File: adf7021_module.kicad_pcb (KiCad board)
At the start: 4 copper layers, 52 x 26 mm, 70 parts, among them J1 Conn_02x10_Counter_Clockwise, J2 Conn_Coaxial, J3 Conn_Coaxial, J4 Conn_02x10_Counter_Clockwise, J5 Conn_Coaxial, J6 Conn_Coaxial, U1 ADF7021, X1 19.68MHz

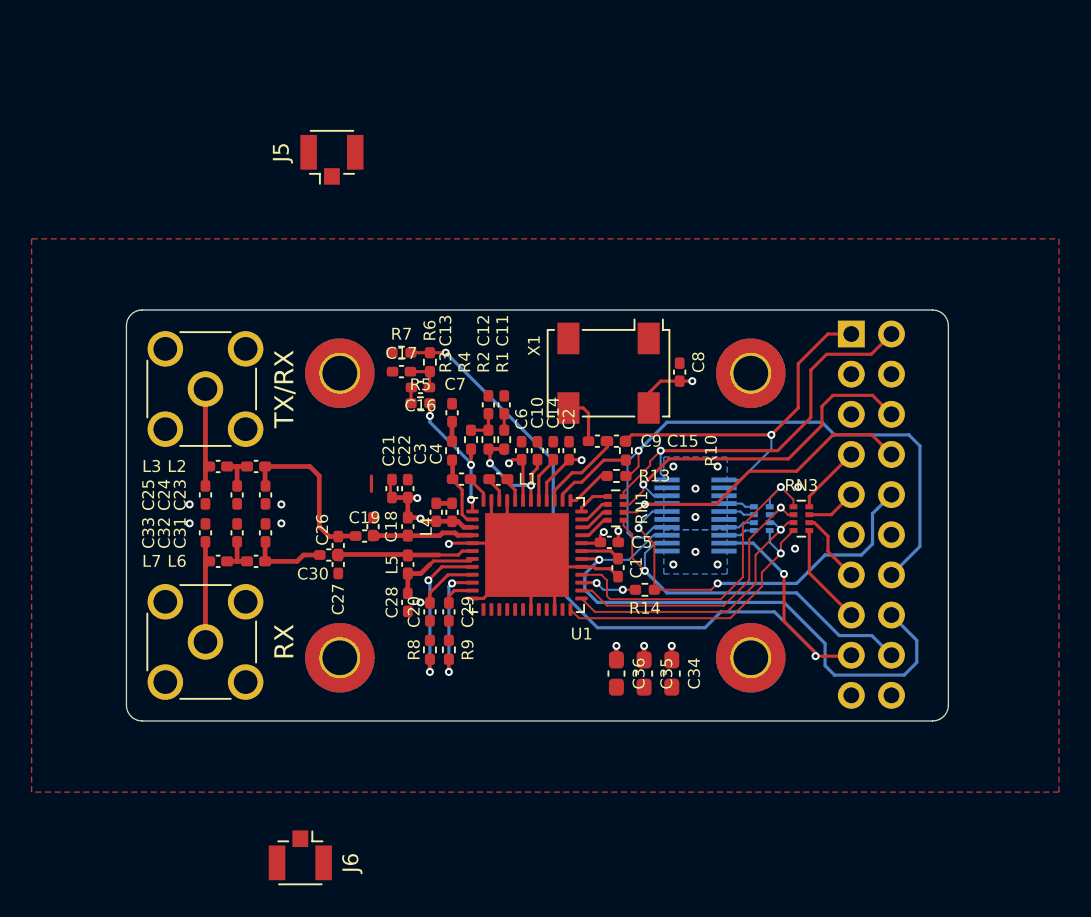
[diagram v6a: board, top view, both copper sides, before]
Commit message: Adding pinout silkscreen
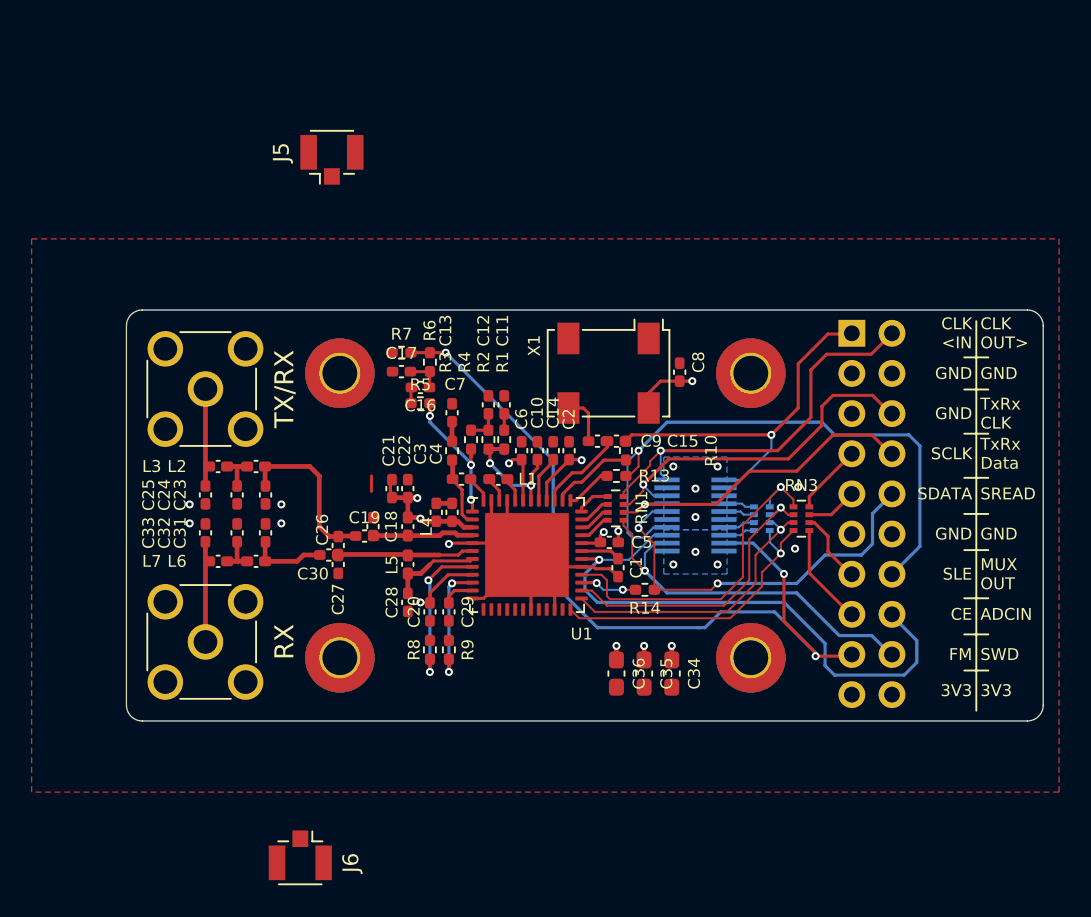
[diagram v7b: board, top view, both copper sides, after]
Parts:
- moved J4 0.06 mm to (151.9, 46.0)
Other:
- board size 52 x 26 mm -> 58 x 26 mm
- board text added: "3V3"
- board text added: "ADCIN"
- board text added: "CE"
- board text added: "CLK <IN"
- board text added: "CLK OUT>"
- board text added: "FM"
- board text added: "GND"
- board text added: "MUX OUT"
- board text added: "SCLK"
- board text added: "SDATA"
- board text added: "SLE"
- board text added: "SREAD"
- board text added: "SWD"
- board text added: "TxRx CLK"
- board text added: "TxRx Data"
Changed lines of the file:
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@@
   (general
     (thickness 1.6)
-    (drawings 20)
+    (drawings 50)
     (tracks 452)
     (zones 0)
@@
   )
   (module Connector_PinSocket_2.54mm:PinSocket_2x10_P2.54mm_Vertical (layer B.Cu)
-    (at 151.86 46.02 180)
+    (at 151.892 45.974 180)
     (descr "Through hole straight socket strip, 2x10, 2.54mm pitch, double cols (from Kicad 4.0.7), script generated")
     (tags "Through hole socket strip THT 2x10 2.54mm double row")
@@
     )
   )
+  (gr_line (start 159.004 47.498) (end 160.528 47.498) (layer F.SilkS) (width 0.12))
+  (gr_line (start 159.004 49.53) (end 160.528 49.53) (layer F.SilkS) (width 0.12))
+  (gr_line (start 159.004 52.324) (end 160.528 52.324) (layer F.SilkS) (width 0.12))
+  (gr_line (start 159.004 55.118) (end 160.528 55.118) (layer F.SilkS) (width 0.12))
+  (gr_line (start 159.004 57.404) (end 160.528 57.404) (layer F.SilkS) (width 0.12))
+  (gr_line (start 159.004 59.69) (end 160.528 59.69) (layer F.SilkS) (width 0.12))
+  (gr_line (start 159.004 62.738) (end 160.528 62.738) (layer F.SilkS) (width 0.12))
+  (gr_line (start 159.004 65.024) (end 160.528 65.024) (layer F.SilkS) (width 0.12))
+  (gr_line (start 159.004 67.31) (end 160.528 67.31) (layer F.SilkS) (width 0.12))
+  (gr_line (start 159.766 45.212) (end 159.766 69.85) (layer F.SilkS) (width 0.12))
+  (gr_text 3V3 (at 160.02 68.58) (layer F.SilkS)
+    (effects (font (size 0.75 0.75) (thickness 0.15)) (justify left))
+  )
+  (gr_text SWD (at 160.02 66.294) (layer F.SilkS)
+    (effects (font (size 0.75 0.75) (thickness 0.15)) (justify left))
+  )
+  (gr_text ADCIN (at 160.02 63.754) (layer F.SilkS)
+    (effects (font (size 0.75 0.75) (thickness 0.15)) (justify left))
+  )
+  (gr_text "MUX\nOUT" (at 160.02 61.214) (layer F.SilkS)
+    (effects (font (size 0.75 0.75) (thickness 0.15)) (justify left))
+  )
+  (gr_text GND (at 160.02 58.674) (layer F.SilkS)
+    (effects (font (size 0.75 0.75) (thickness 0.15)) (justify left))
+  )
+  (gr_text SREAD (at 160.02 56.134) (layer F.SilkS)
+    (effects (font (size 0.75 0.75) (thickness 0.15)) (justify left))
+  )
+  (gr_text "TxRx\nData" (at 160.02 53.594) (layer F.SilkS)
+    (effects (font (size 0.75 0.75) (thickness 0.15)) (justify left))
+  )
+  (gr_text "TxRx\nCLK" (at 160.02 51.054) (layer F.SilkS)
+    (effects (font (size 0.75 0.75) (thickness 0.15)) (justify left))
+  )
+  (gr_text GND (at 160.02 48.514) (layer F.SilkS)
+    (effects (font (size 0.75 0.75) (thickness 0.15)) (justify left))
+  )
+  (gr_text "CLK\nOUT>" (at 160.02 45.974) (layer F.SilkS)
+    (effects (font (size 0.75 0.75) (thickness 0.15)) (justify left))
+  )
+  (gr_text 3V3 (at 159.512 68.58) (layer F.SilkS)
+    (effects (font (size 0.75 0.75) (thickness 0.15)) (justify right))
+  )
+  (gr_text FM (at 159.512 66.294) (layer F.SilkS)
+    (effects (font (size 0.75 0.75) (thickness 0.15)) (justify right))
+  )
+  (gr_text CE (at 159.512 63.754) (layer F.SilkS)
+    (effects (font (size 0.75 0.75) (thickness 0.15)) (justify right))
+  )
+  (gr_text SLE (at 159.512 61.214) (layer F.SilkS)
+    (effects (font (size 0.75 0.75) (thickness 0.15)) (justify right))
+  )
+  (gr_text GND (at 159.512 58.674) (layer F.SilkS)
+    (effects (font (size 0.75 0.75) (thickness 0.15)) (justify right))
+  )
+  (gr_text SDATA (at 159.512 56.134) (layer F.SilkS)
+    (effects (font (size 0.75 0.75) (thickness 0.15)) (justify right))
+  )
+  (gr_text SCLK (at 159.512 53.594) (layer F.SilkS)
+    (effects (font (size 0.75 0.75) (thickness 0.15)) (justify right))
+  )
+  (gr_text GND (at 159.512 51.054) (layer F.SilkS)
+    (effects (font (size 0.75 0.75) (thickness 0.15)) (justify right))
+  )
+  (gr_text GND (at 159.512 48.514) (layer F.SilkS)
+    (effects (font (size 0.75 0.75) (thickness 0.15)) (justify right))
+  )
+  (gr_text "CLK\n<IN" (at 159.512 45.974) (layer F.SilkS)
+    (effects (font (size 0.75 0.75) (thickness 0.15)) (justify right))
+  )
   (gr_text RX (at 116 65.5 90) (layer F.SilkS)
     (effects (font (size 1.2 1.2) (thickness 0.25)))
@@
     (arrow2b (pts (xy 119.5 74.5) (xy 120.626504 73.913579)))
   )
-  (gr_arc (start 157 69.5) (end 157 70.5) (angle -90) (layer Edge.Cuts) (width 0.05))
-  (gr_arc (start 157 45.5) (end 158 45.5) (angle -90) (layer Edge.Cuts) (width 0.05))
+  (gr_arc (start 163 69.5) (end 163 70.5) (angle -90) (layer Edge.Cuts) (width 0.05))
+  (gr_arc (start 163 45.5) (end 164 45.5) (angle -90) (layer Edge.Cuts) (width 0.05))
   (gr_arc (start 107 45.5) (end 107 44.5) (angle -90) (layer Edge.Cuts) (width 0.05))
   (gr_arc (start 107 69.5) (end 106 69.5) (angle -90) (layer Edge.Cuts) (width 0.05))
@@
     (arrow2b (pts (xy 172.5 70.5) (xy 171.913579 69.373496)))
   )
-  (gr_line (start 158 69.5) (end 158 45.5) (layer Edge.Cuts) (width 0.05))
+  (gr_line (start 164 69.5) (end 164 45.5) (layer Edge.Cuts) (width 0.05))
   (gr_text "12mil / 0.3mm \ntrace should be 50Ωish" (at 105.9 39.2) (layer Dwgs.User)
     (effects (font (size 1.5 1.5) (thickness 0.3)) (justify left))
@@
     (effects (font (size 1.5 1.5) (thickness 0.3)) (justify left))
   )
-  (dimension 52 (width 0.15) (layer Dwgs.User)
-    (gr_text "52.000 mm" (at 132 79.3) (layer Dwgs.User)
+  (dimension 58 (width 0.15) (layer Dwgs.User)
+    (gr_text "58.000 mm" (at 135 79.3) (layer Dwgs.User)
       (effects (font (size 1 1) (thickness 0.15)))
     )
     (feature1 (pts (xy 106 70.5) (xy 106 78.586421)))
-    (feature2 (pts (xy 158 70.5) (xy 158 78.586421)))
-    (crossbar (pts (xy 158 78) (xy 106 78)))
+    (feature2 (pts (xy 164 70.5) (xy 164 78.586421)))
+    (crossbar (pts (xy 164 78) (xy 106 78)))
     (arrow1a (pts (xy 106 78) (xy 107.126504 77.413579)))
     (arrow1b (pts (xy 106 78) (xy 107.126504 78.586421)))
-    (arrow2a (pts (xy 158 78) (xy 156.873496 77.413579)))
-    (arrow2b (pts (xy 158 78) (xy 156.873496 78.586421)))
+    (arrow2a (pts (xy 164 78) (xy 162.873496 77.413579)))
+    (arrow2b (pts (xy 164 78) (xy 162.873496 78.586421)))
   )
-  (gr_line (start 107 70.5) (end 157 70.5) (layer Edge.Cuts) (width 0.05))
+  (gr_line (start 107 70.5) (end 163 70.5) (layer Edge.Cuts) (width 0.05))
   (gr_line (start 106 45.5) (end 106 69.5) (layer Edge.Cuts) (width 0.05))
-  (gr_line (start 157 44.5) (end 107 44.5) (layer Edge.Cuts) (width 0.05))
+  (gr_line (start 163 44.5) (end 107 44.5) (layer Edge.Cuts) (width 0.05))
   (segment (start 122.7 55.9725) (end 122.7 55) (width 0.2) (layer F.Cu) (net 1))
   (segment (start 121.5 55.9725) (end 121.5 55) (width 0.2) (layer F.Cu) (net 1))

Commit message: Moving mounting holes to make room for U.FL's
 * 0 unrouted traces
 * DRC clear
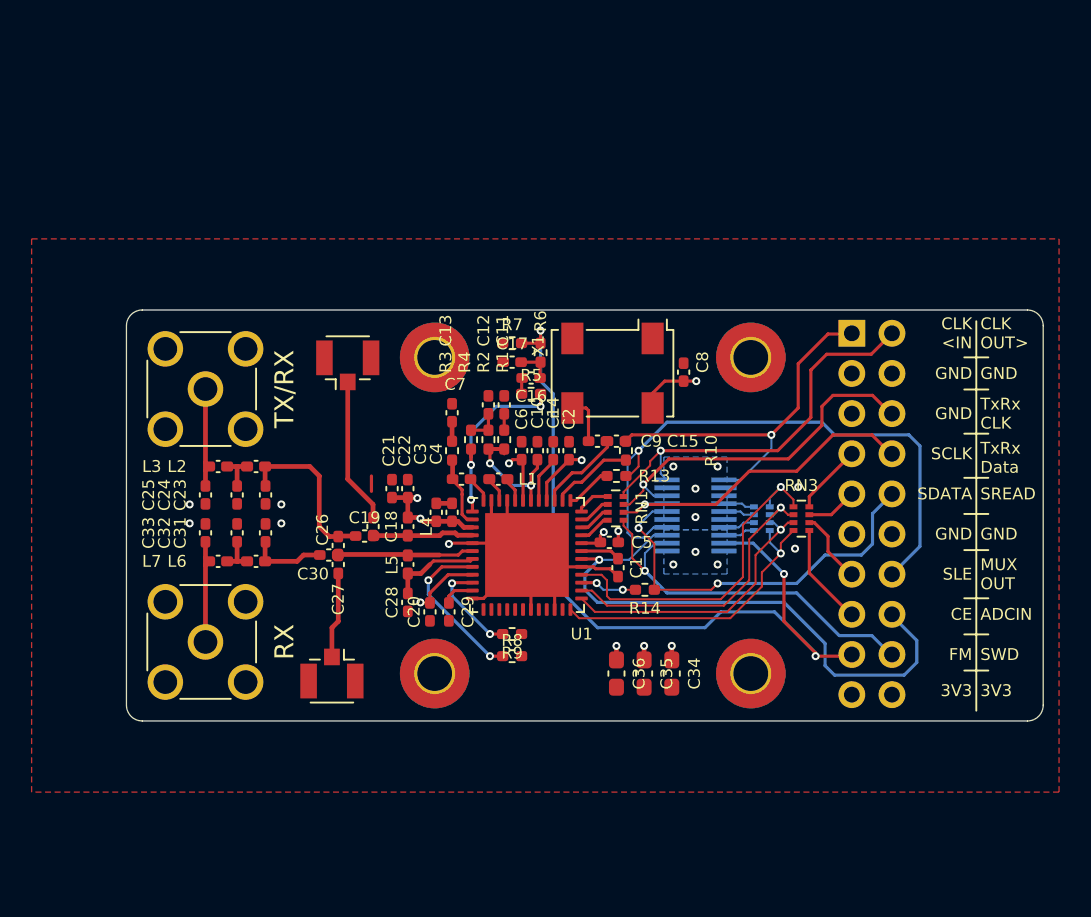
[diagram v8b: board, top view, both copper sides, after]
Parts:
- moved J5 13.0 mm to (120.0, 48.0)
- moved J6 11.7 mm to (119.0, 67.5)
- moved C16 7.03 mm to (131.6, 48.8)
- moved C17 7.03 mm to (130.4, 47.8)
- moved R5 7.03 mm to (131.6, 49.8)
- moved R7 7.03 mm to (130.4, 46.6)
- moved R6 7.03 mm to (132.2, 47.2)
- moved H1 6.08 mm to (125.5, 47.5)
- moved H2 6.08 mm to (125.5, 67.5)
- moved R8 5.22 mm to (130.4, 66.4), turned to 0 degrees
- moved R9 4.12 mm to (130.4, 65.0), turned to 0 degrees
- moved H3 1.00 mm to (145.5, 47.5)
- moved H4 1.00 mm to (145.5, 67.5)
- moved C8 0.25 mm to (141.2, 48.4)
- moved X1 0.25 mm to (136.8, 48.5)
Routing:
- net Net-(C18-Pad1): track 0.00 -> 9.25 mm
- net Net-(C27-Pad2): track 0.00 -> 5.45 mm
- net /VCOIN: track 9.47 -> 12.6 mm
- net /RSET: track 7.80 -> 6.32 mm
- net FM_MOD: track 52.0 -> 50.7 mm
- net GND: track 35.9 -> 35.0 mm
- net /R_LNA: track 9.79 -> 10.5 mm
